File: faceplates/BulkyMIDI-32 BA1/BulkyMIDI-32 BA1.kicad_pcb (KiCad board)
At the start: 2 copper layers, 100 x 100 mm, 8 parts, among them M1 Mounting, M2 Mounting, M3 Mounting, M4 Mounting

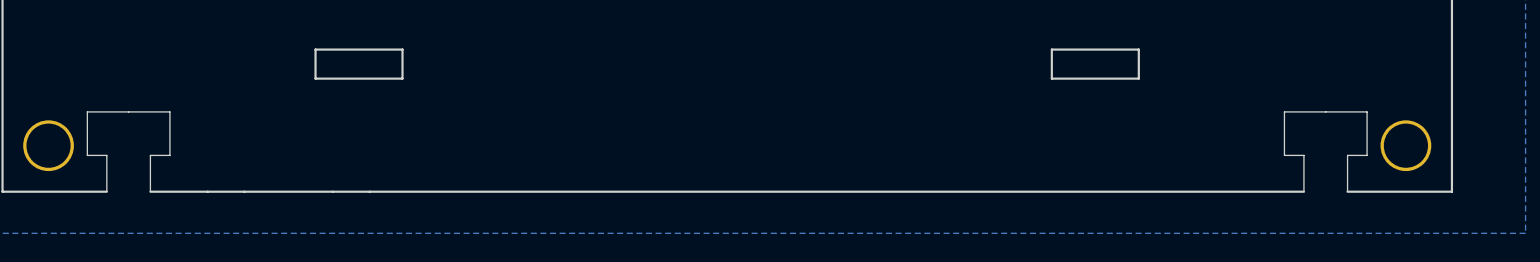
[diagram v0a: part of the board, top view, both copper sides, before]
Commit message: Changed BA1 to match new layout
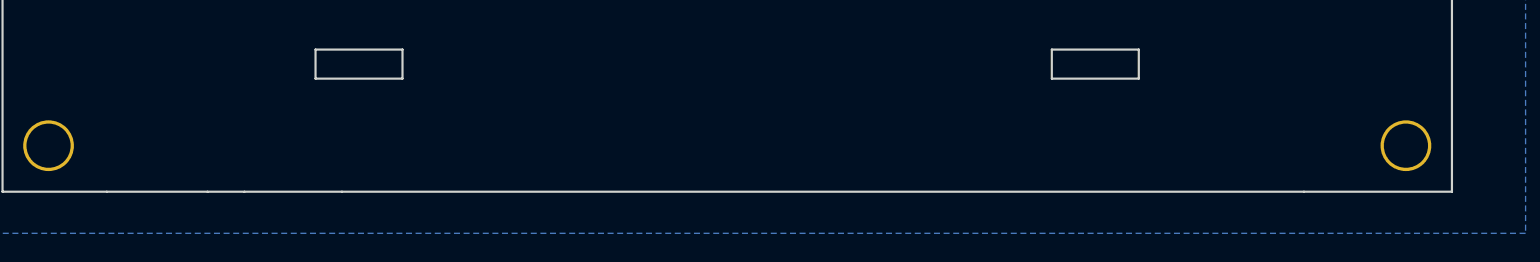
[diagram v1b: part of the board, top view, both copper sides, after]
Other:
- outline, holes or cut-outs redrawn
- board text removed: "POWER"
